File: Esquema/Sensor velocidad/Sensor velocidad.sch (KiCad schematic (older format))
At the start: 49 parts

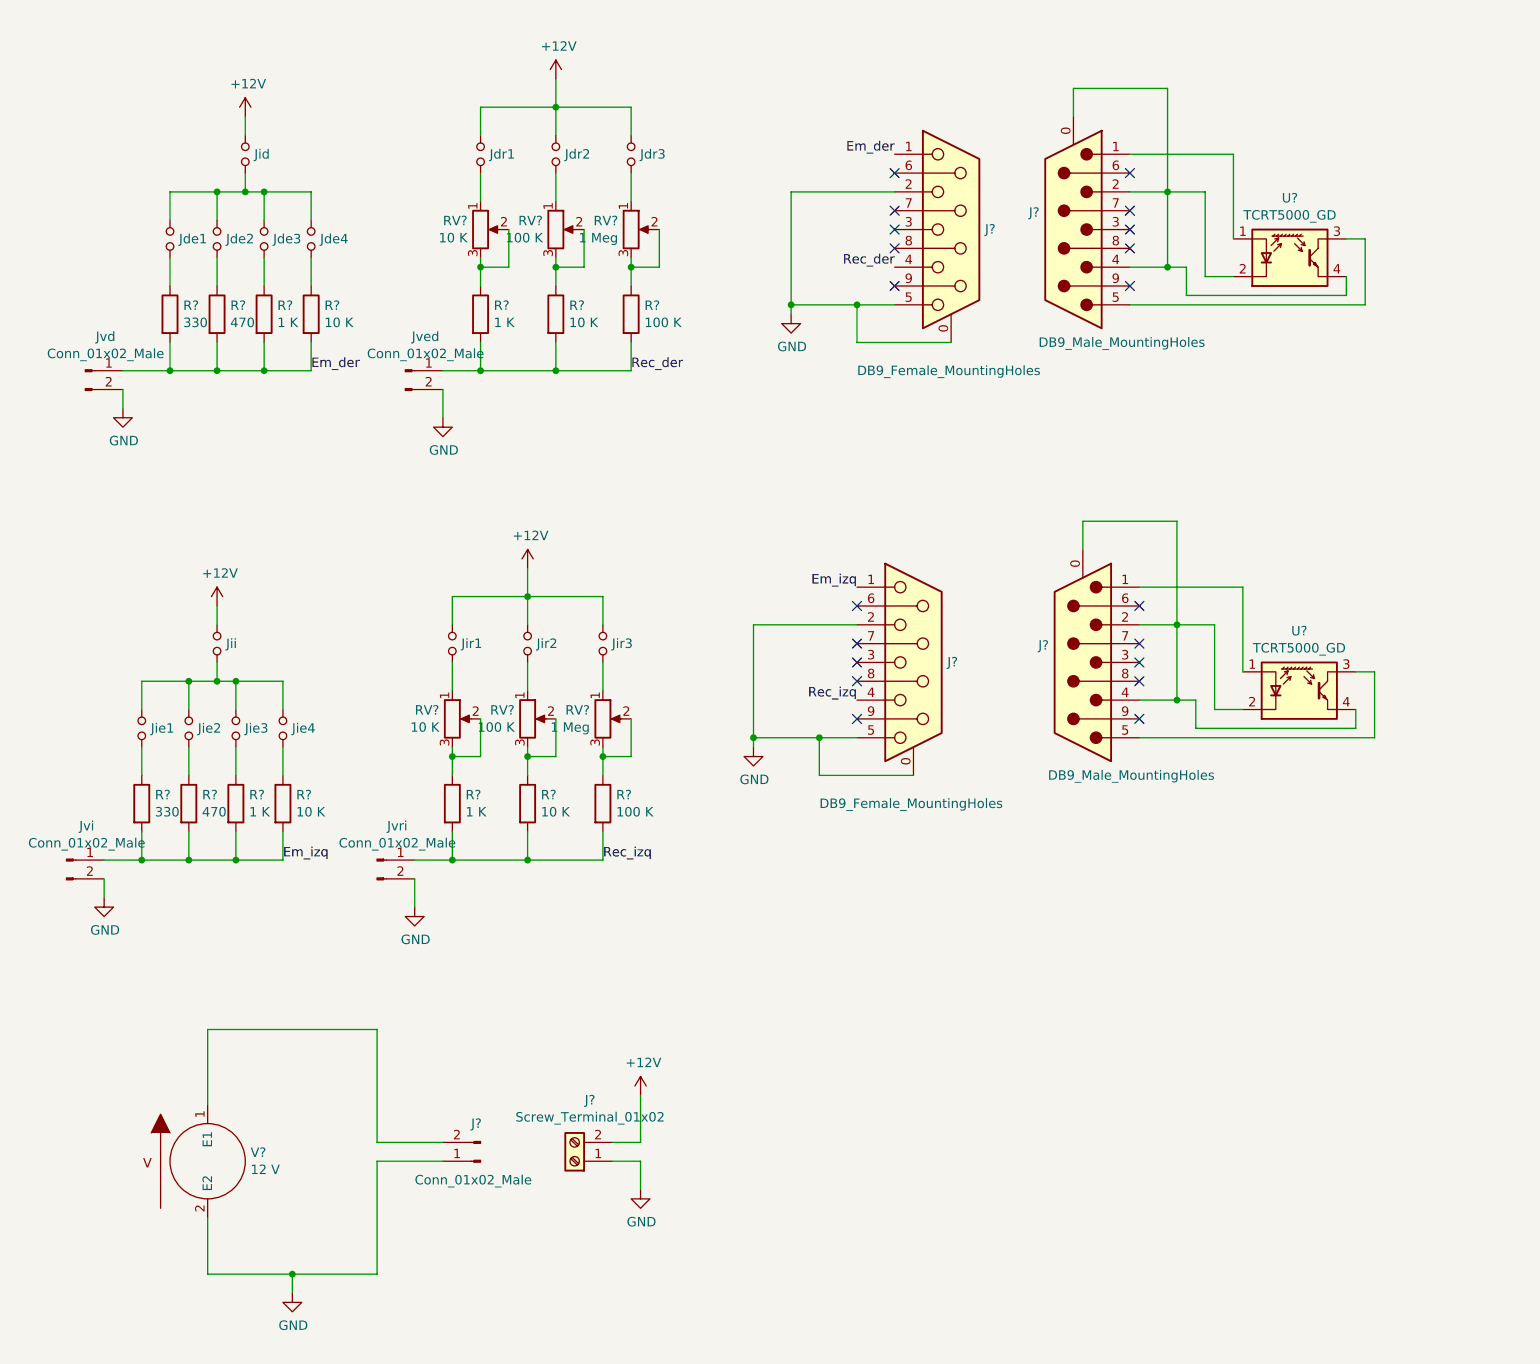
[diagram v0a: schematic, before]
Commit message: Primera versión de esquemático para sensado de desbalanceo en ambos lados
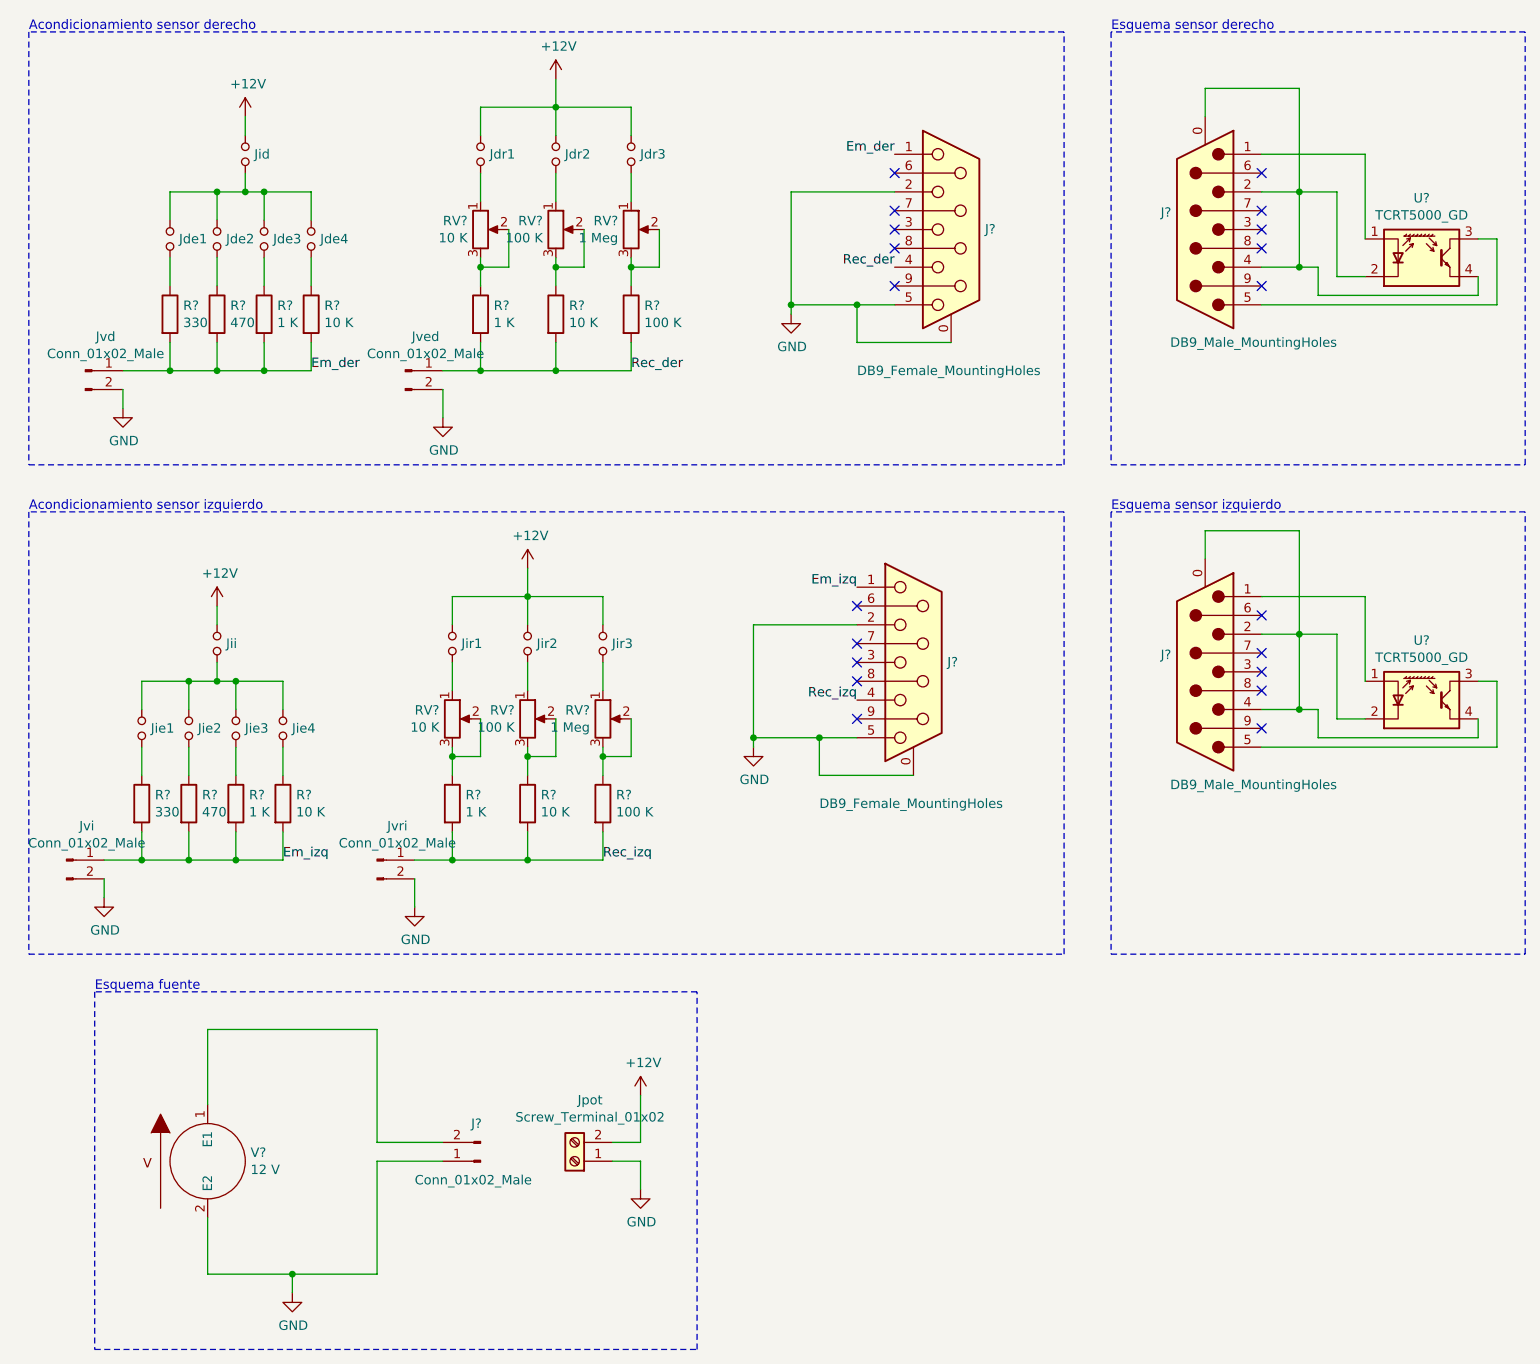
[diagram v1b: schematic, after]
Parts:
- gave numbers to parts that had none: 1
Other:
- note added: "Acondicionamiento sensor derecho"
- note added: "Acondicionamiento sensor izquierdo"
- note added: "Esquema fuente"
- note added: "Esquema sensor derecho"
- note added: "Esquema sensor izquierdo"
- moved on the sheet: J?, U?
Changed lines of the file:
@@
 L Sensor_vel_bib:TCRT5000_GD U?
 U 1 1 5D8A6EC4
-P 7300 1800
-F 0 "U?" H 7300 2117 50  0000 C CNN
-F 1 "TCRT5000_GD" H 7300 2026 50  0000 C CNN
-F 2 "" H 7300 1600 50  0001 C CNN
-F 3 "https://www.vishay.com/docs/83760/tcrt5000.pdf" H 7300 1900 50  0001 C CNN
-	1    7300 1800
+P 8000 1800
+F 0 "U?" H 8000 2117 50  0000 C CNN
+F 1 "TCRT5000_GD" H 8000 2026 50  0000 C CNN
+F 2 "" H 8000 1600 50  0001 C CNN
+F 3 "https://www.vishay.com/docs/83760/tcrt5000.pdf" H 8000 1900 50  0001 C CNN
+	1    8000 1800
 	1    0    0    -1
 $EndComp
@@
 L Connector:DB9_Male_MountingHoles J?
 U 1 1 5EC0C521
-P 6150 1650
-F 0 "J?" H 6330 1559 50  0000 L CNN
-F 1 "DB9_Male_MountingHoles" H 5450 2250 50  0000 L CNN
-F 2 "" H 6150 1650 50  0001 C CNN
-F 3 " ~" H 6150 1650 50  0001 C CNN
-	1    6150 1650
+P 6850 1650
+F 0 "J?" H 7030 1559 50  0000 L CNN
+F 1 "DB9_Male_MountingHoles" H 6150 2250 50  0000 L CNN
+F 2 "" H 6850 1650 50  0001 C CNN
+F 3 " ~" H 6850 1650 50  0001 C CNN
+	1    6850 1650
 	-1   0    0    1
 $EndComp
 $Comp
-L Connector:Screw_Terminal_01x02 J?
+L Connector:Screw_Terminal_01x02 Jpot
 U 1 1 5EC730C8
 P 3500 6600
-F 0 "J?" H 3418 6275 50  0000 C CNN
+F 0 "Jpot" H 3418 6275 50  0000 C CNN
 F 1 "Screw_Terminal_01x02" H 3418 6366 50  0000 C CNN
 F 2 "" H 3500 6600 50  0001 C CNN
@@
 	2800 2650 2800 2500
 Wire Wire Line
-	6450 1250 7000 1250
-Wire Wire Line
-	7000 1250 7000 1700
-Wire Wire Line
-	6450 1450 6650 1450
-Wire Wire Line
-	6850 1450 6850 1900
-Wire Wire Line
-	6850 1900 7000 1900
-Wire Wire Line
-	7600 1900 7600 2000
-Wire Wire Line
-	6750 2000 6750 1850
-Wire Wire Line
-	6750 1850 6650 1850
-Wire Wire Line
-	6450 2050 7700 2050
-Wire Wire Line
-	7700 2050 7700 1700
-Wire Wire Line
-	7700 1700 7600 1700
-Wire Wire Line
-	6150 1050 6150 900
-Wire Wire Line
-	6150 900  6650 900
-Wire Wire Line
-	6650 900  6650 1450
-Connection ~ 6650 1450
-Wire Wire Line
-	6650 1450 6850 1450
-Wire Wire Line
-	7600 2000 6750 2000
-Wire Wire Line
-	6650 1450 6650 1850
-Connection ~ 6650 1850
-Wire Wire Line
-	6650 1850 6450 1850
+	7150 1250 7700 1250
+Wire Wire Line
+	7700 1250 7700 1700
+Wire Wire Line
+	7150 1450 7350 1450
+Wire Wire Line
+	7550 1450 7550 1900
+Wire Wire Line
+	7550 1900 7700 1900
+Wire Wire Line
+	8300 1900 8300 2000
+Wire Wire Line
+	7450 2000 7450 1850
+Wire Wire Line
+	7450 1850 7350 1850
+Wire Wire Line
+	7150 2050 8400 2050
+Wire Wire Line
+	8400 2050 8400 1700
+Wire Wire Line
+	8400 1700 8300 1700
+Wire Wire Line
+	6850 1050 6850 900
+Wire Wire Line
+	6850 900  7350 900
+Wire Wire Line
+	7350 900  7350 1450
+Connection ~ 7350 1450
+Wire Wire Line
+	7350 1450 7550 1450
+Wire Wire Line
+	8300 2000 7450 2000
+Wire Wire Line
+	7350 1450 7350 1850
+Connection ~ 7350 1850
+Wire Wire Line
+	7350 1850 7150 1850
 Text Label 2100 2400 0    50   ~ 0
 Em_der
@@
 NoConn ~ 5200 1750
 NoConn ~ 5200 1950
-NoConn ~ 6450 1350
-NoConn ~ 6450 1550
-NoConn ~ 6450 1650
-NoConn ~ 6450 1750
-NoConn ~ 6450 1950
+NoConn ~ 7150 1350
+NoConn ~ 7150 1550
+NoConn ~ 7150 1650
+NoConn ~ 7150 1750
+NoConn ~ 7150 1950
 Wire Wire Line
 	4650 2050 5000 2050
@@
 L Sensor_vel_bib:TCRT5000_GD U?
 U 1 1 5ED56EC2
-P 7350 4100
-F 0 "U?" H 7350 4417 50  0000 C CNN
-F 1 "TCRT5000_GD" H 7350 4326 50  0000 C CNN
-F 2 "" H 7350 3900 50  0001 C CNN
-F 3 "https://www.vishay.com/docs/83760/tcrt5000.pdf" H 7350 4200 50  0001 C CNN
-	1    7350 4100
+P 8000 4150
+F 0 "U?" H 8000 4467 50  0000 C CNN
+F 1 "TCRT5000_GD" H 8000 4376 50  0000 C CNN
+F 2 "" H 8000 3950 50  0001 C CNN
+F 3 "https://www.vishay.com/docs/83760/tcrt5000.pdf" H 8000 4250 50  0001 C CNN
+	1    8000 4150
 	1    0    0    -1
 $EndComp
@@
 L Connector:DB9_Male_MountingHoles J?
 U 1 1 5ED56F30
-P 6200 3950
-F 0 "J?" H 6380 3859 50  0000 L CNN
-F 1 "DB9_Male_MountingHoles" H 5500 4550 50  0000 L CNN
-F 2 "" H 6200 3950 50  0001 C CNN
-F 3 " ~" H 6200 3950 50  0001 C CNN
-	1    6200 3950
+P 6850 4000
+F 0 "J?" H 7030 3909 50  0000 L CNN
+F 1 "DB9_Male_MountingHoles" H 6150 4600 50  0000 L CNN
+F 2 "" H 6850 4000 50  0001 C CNN
+F 3 " ~" H 6850 4000 50  0001 C CNN
+	1    6850 4000
 	-1   0    0    1
 $EndComp
@@
 	2650 5250 2650 5100
 Wire Wire Line
-	6500 3550 7050 3550
-Wire Wire Line
-	7050 3550 7050 4000
-Wire Wire Line
-	6500 3750 6700 3750
-Wire Wire Line
-	6900 3750 6900 4200
-Wire Wire Line
-	6900 4200 7050 4200
-Wire Wire Line
-	7650 4200 7650 4300
-Wire Wire Line
-	6800 4300 6800 4150
-Wire Wire Line
-	6800 4150 6700 4150
-Wire Wire Line
-	6500 4350 7750 4350
-Wire Wire Line
-	7750 4350 7750 4000
-Wire Wire Line
-	7750 4000 7650 4000
-Wire Wire Line
-	6200 3350 6200 3200
-Wire Wire Line
-	6200 3200 6700 3200
-Wire Wire Line
-	6700 3200 6700 3750
-Connection ~ 6700 3750
-Wire Wire Line
-	6700 3750 6900 3750
-Wire Wire Line
-	7650 4300 6800 4300
-Wire Wire Line
-	6700 3750 6700 4150
-Connection ~ 6700 4150
-Wire Wire Line
-	6700 4150 6500 4150
+	7150 3600 7700 3600
+Wire Wire Line
+	7700 3600 7700 4050
+Wire Wire Line
+	7150 3800 7350 3800
+Wire Wire Line
+	7550 3800 7550 4250
+Wire Wire Line
+	7550 4250 7700 4250
+Wire Wire Line
+	8300 4250 8300 4350
+Wire Wire Line
+	7450 4350 7450 4200
+Wire Wire Line
+	7450 4200 7350 4200
+Wire Wire Line
+	7150 4400 8400 4400
+Wire Wire Line
+	8400 4400 8400 4050
+Wire Wire Line
+	8400 4050 8300 4050
+Wire Wire Line
+	6850 3400 6850 3250
+Wire Wire Line
+	6850 3250 7350 3250
+Wire Wire Line
+	7350 3250 7350 3800
+Connection ~ 7350 3800
+Wire Wire Line
+	7350 3800 7550 3800
+Wire Wire Line
+	8300 4350 7450 4350
+Wire Wire Line
+	7350 3800 7350 4200
+Connection ~ 7350 4200
+Wire Wire Line
+	7350 4200 7150 4200
 Text Label 1950 5000 0    50   ~ 0
 Em_izq
@@
 NoConn ~ 5000 4050
 NoConn ~ 5000 4250
-NoConn ~ 6500 3650
-NoConn ~ 6500 3850
-NoConn ~ 6500 3950
-NoConn ~ 6500 4050
-NoConn ~ 6500 4250
+NoConn ~ 7150 3700
+NoConn ~ 7150 3900
+NoConn ~ 7150 4000
+NoConn ~ 7150 4100
+NoConn ~ 7150 4300
 Wire Wire Line
 	4450 4350 4800 4350
@@
 	1000 5000 1200 5000
 Connection ~ 1200 5000
+Wire Notes Line
+	600  600  600  2900
+Wire Notes Line
+	600  2900 6100 2900
+Wire Notes Line
+	6100 2900 6100 600
+Wire Notes Line
+	6100 600  600  600
+Wire Notes Line
+	6350 600  6350 2900
+Wire Notes Line
+	6350 2900 8550 2900
+Wire Notes Line
+	8550 2900 8550 600
+Wire Notes Line
+	8550 600  6350 600
+Wire Notes Line
+	600  3150 600  5500
+Wire Notes Line
+	600  5500 6100 5500
+Wire Notes Line
+	6100 5500 6100 3150
+Wire Notes Line
+	6100 3150 600  3150
+Wire Notes Line
+	6350 3150 6350 5500
+Wire Notes Line
+	6350 5500 8550 5500
+Wire Notes Line
+	8550 5500 8550 3150
+Wire Notes Line
+	8550 3150 6350 3150
+Wire Notes Line
+	950  5700 950  7600
+Wire Notes Line
+	950  7600 4150 7600
+Wire Notes Line
+	4150 7600 4150 5700
+Wire Notes Line
+	4150 5700 950  5700
+Text Notes 600  600  0    50   ~ 0
+Acondicionamiento sensor derecho
+Text Notes 6350 600  0    50   ~ 0
+Esquema sensor derecho
+Text Notes 600  3150 0    50   ~ 0
+Acondicionamiento sensor izquierdo
+Text Notes 6350 3150 0    50   ~ 0
+Esquema sensor izquierdo
+Text Notes 950  5700 0    50   ~ 0
+Esquema fuente
 $EndSCHEMATC

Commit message: Esquema con función annotate ejecutada
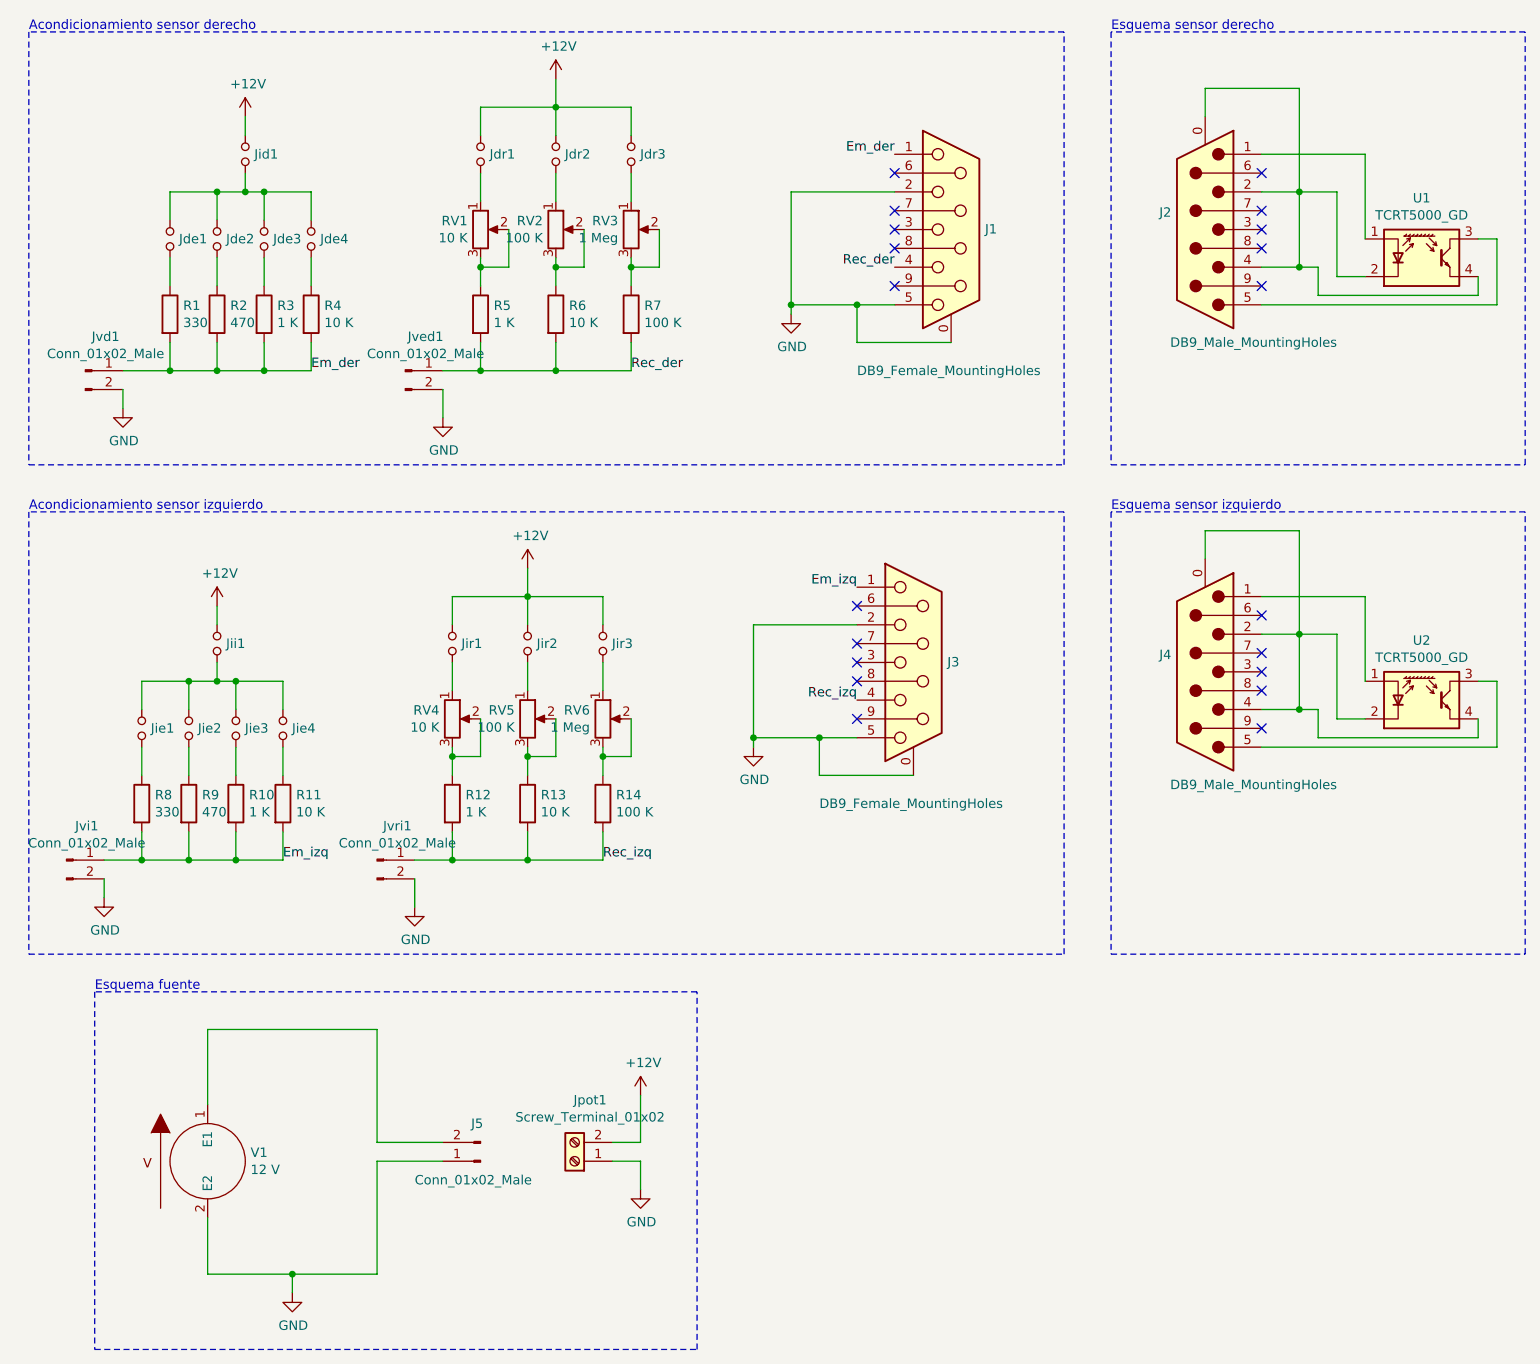
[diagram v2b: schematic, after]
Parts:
- gave numbers to parts that had none: 28
- renumbered Jid to Jid1, Jii to Jii1, Jpot to Jpot1, Jvd to Jvd1, Jved to Jved1, Jvi to Jvi1, Jvri to Jvri1
